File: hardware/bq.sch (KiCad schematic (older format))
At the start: 39 parts, among them Q11 BUK762R6-60E, Q12 BUK762R6-60E, Q13 Si2319DS, U1 bq7693002DBT, U2 BUK9Y43-60E

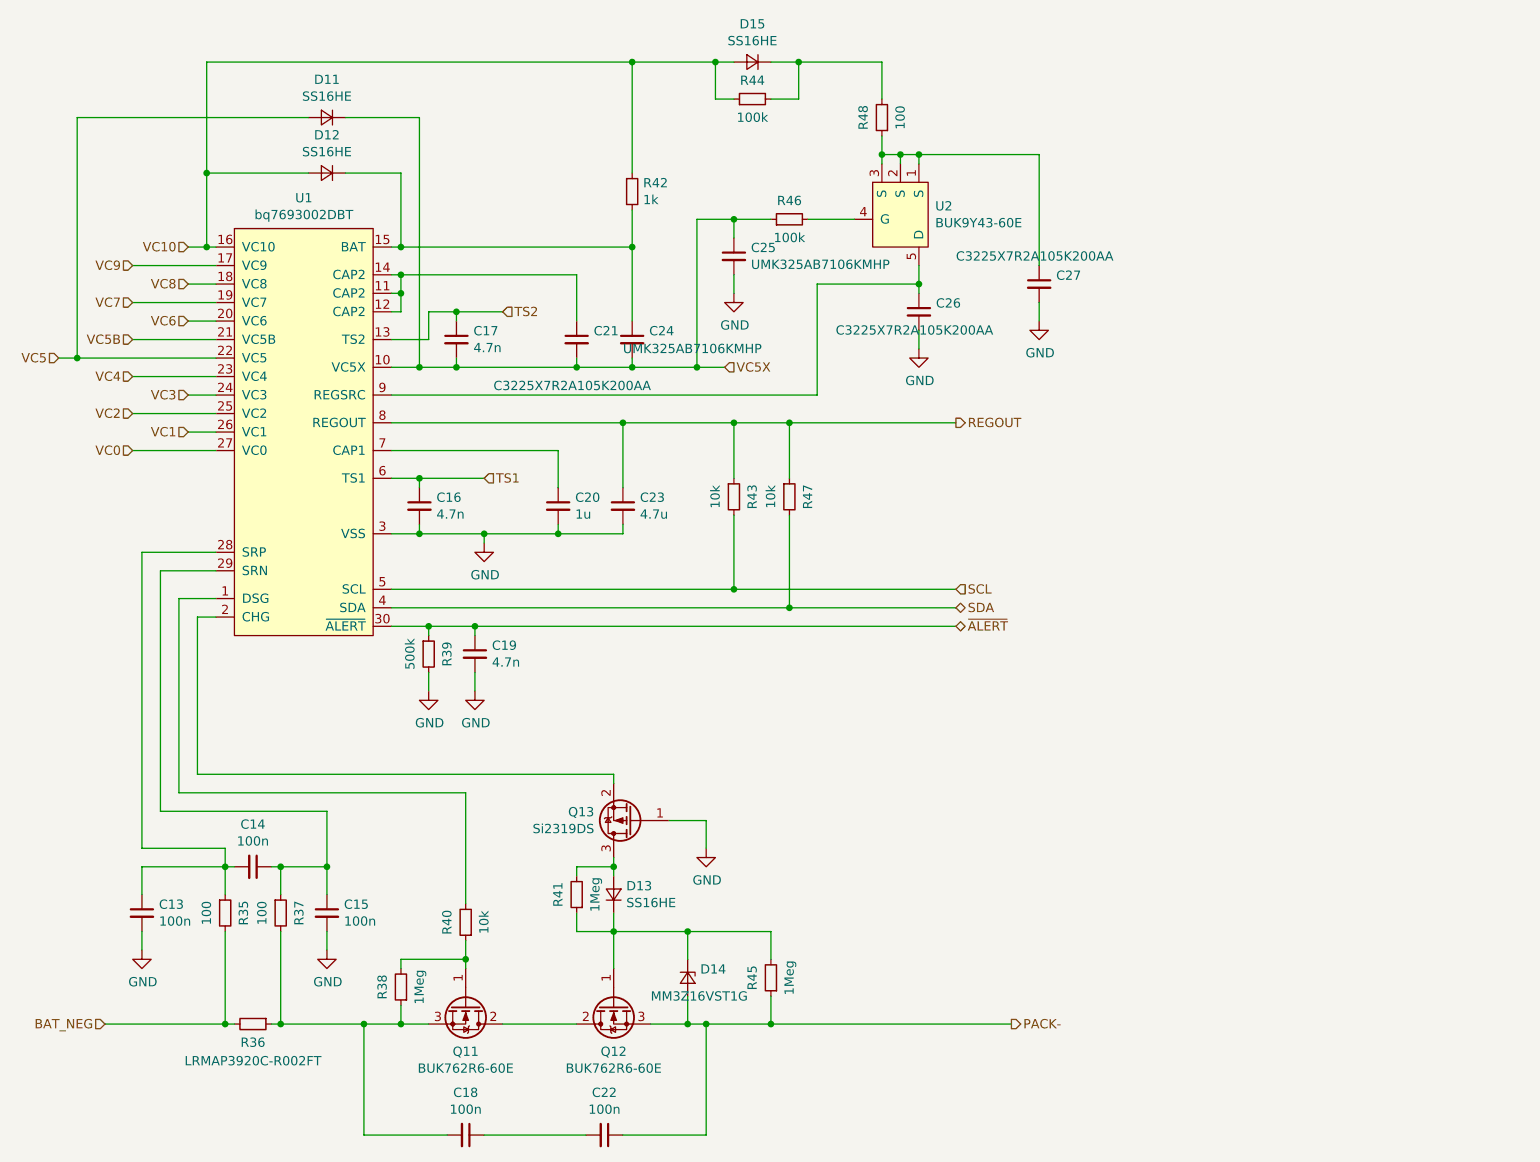
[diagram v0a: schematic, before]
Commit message: finish clean-up and part assignment
Signed-off-by: Ene Alexandru <ene.alexandru@gmail.com>
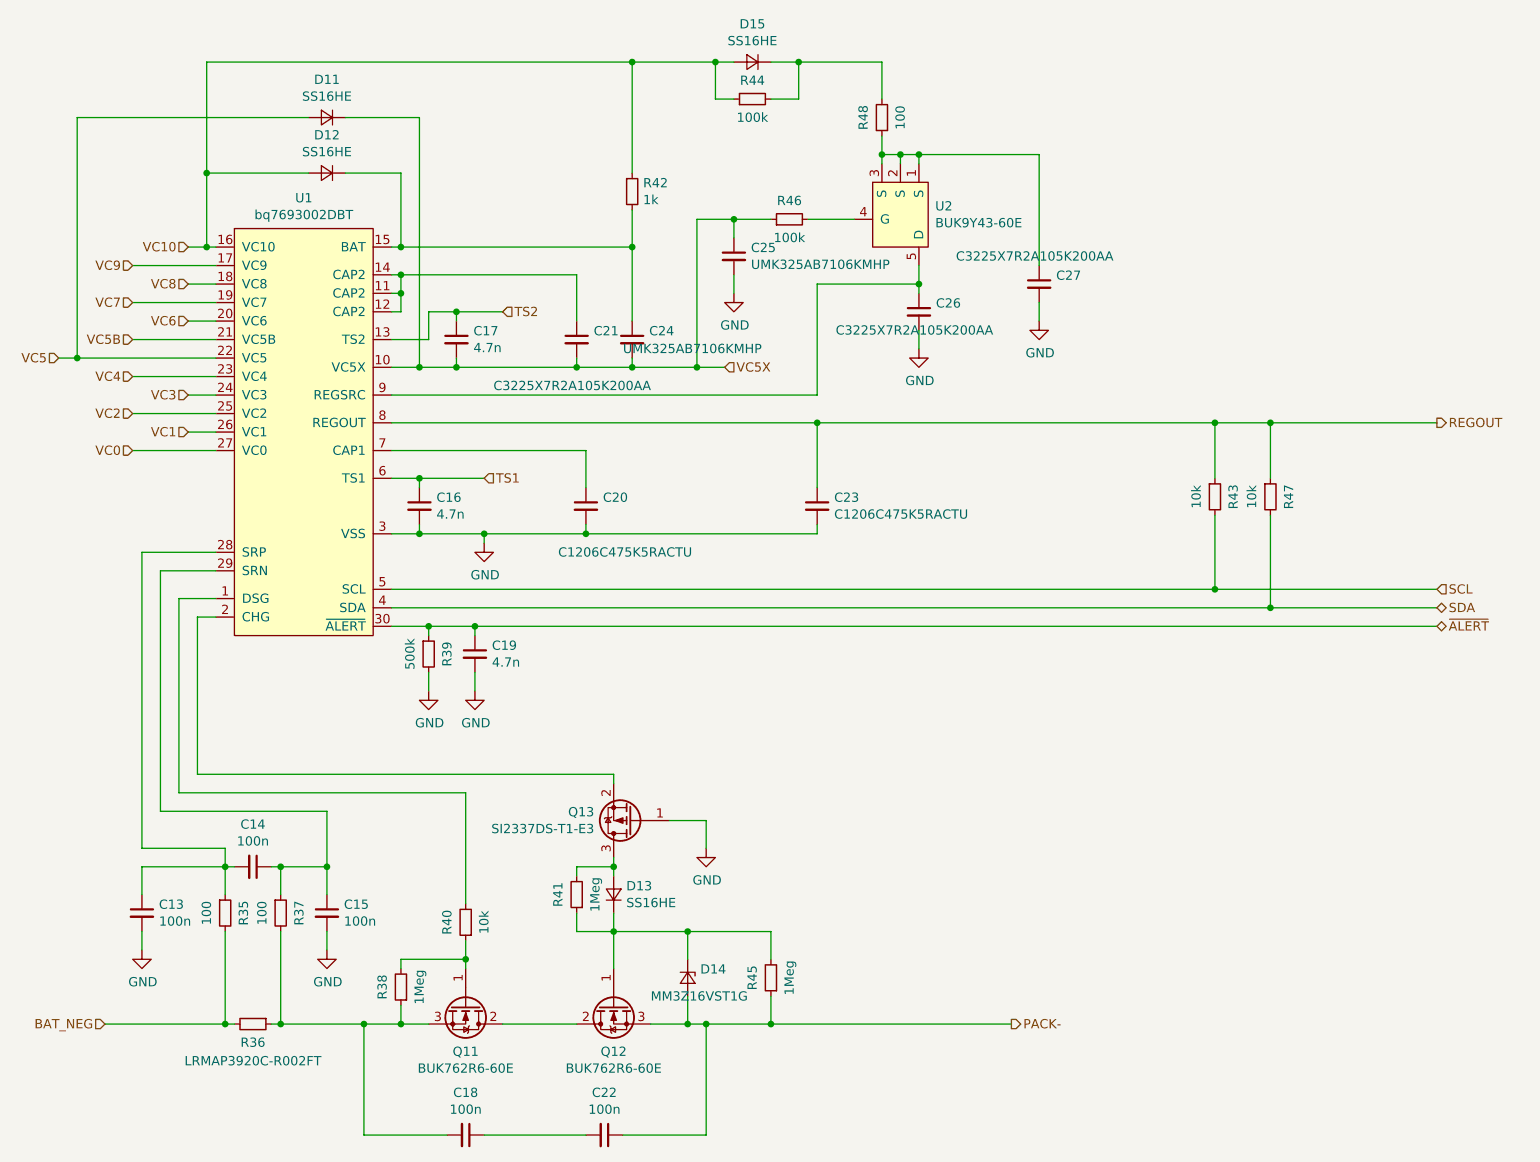
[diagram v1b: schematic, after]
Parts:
- C20: value 1u -> C1206C475K5RACTU
- C23: value 4.7u -> C1206C475K5RACTU
- Q13: value Si2319DS -> SI2337DS-T1-E3
- R36: footprint (none) -> bms_10s:LRMAP3920C-R002FT
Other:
- moved on the sheet: C20, C23, R43, R47
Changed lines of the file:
@@
 Wire Wire Line
 	5450 2050 5450 2100
-Wire Wire Line
-	2600 2800 3850 2800
 $Comp
 L Device:C_Small C16
@@
 L Device:C_Small C20
 U 1 1 5DF08E44
-P 3500 3250
-F 0 "C20" H 3592 3296 50  0000 L CNN
-F 1 "1u" H 3592 3205 50  0000 L CNN
-F 2 "Capacitor_SMD:C_0805_2012Metric_Pad1.15x1.40mm_HandSolder" H 3500 3250 50  0001 C CNN
-F 3 "~" H 3500 3250 50  0001 C CNN
-	1    3500 3250
+P 3650 3250
+F 0 "C20" H 3742 3296 50  0000 L CNN
+F 1 "C1206C475K5RACTU" H 3500 3000 50  0000 L CNN
+F 2 "Capacitor_SMD:C_0805_2012Metric_Pad1.15x1.40mm_HandSolder" H 3650 3250 50  0001 C CNN
+F 3 "~" H 3650 3250 50  0001 C CNN
+	1    3650 3250
 	1    0    0    -1
 $EndComp
@@
 	2750 3400 3100 3400
 Wire Wire Line
-	3500 3400 3500 3350
+	3650 3400 3650 3350
 Connection ~ 2750 3400
 $Comp
@@
 Wire Wire Line
 	3100 3450 3100 3400
-Connection ~ 3100 3400
-Wire Wire Line
-	3100 3400 3500 3400
-Wire Wire Line
-	2600 2950 3500 2950
-Wire Wire Line
-	3500 2950 3500 3150
+Wire Wire Line
+	3650 2950 3650 3150
 Wire Wire Line
 	2600 3100 2750 3100
@@
 L Device:C_Small C23
 U 1 1 5DF13B4E
-P 3850 3250
-F 0 "C23" H 3942 3296 50  0000 L CNN
-F 1 "4.7u" H 3942 3205 50  0000 L CNN
-F 2 "Capacitor_SMD:C_0805_2012Metric_Pad1.15x1.40mm_HandSolder" H 3850 3250 50  0001 C CNN
-F 3 "~" H 3850 3250 50  0001 C CNN
-	1    3850 3250
-	1    0    0    -1
-$EndComp
-Wire Wire Line
-	3850 3350 3850 3400
-Wire Wire Line
-	3850 3400 3500 3400
-Connection ~ 3500 3400
-Wire Wire Line
-	3850 3150 3850 2800
-Connection ~ 3850 2800
+P 4900 3250
+F 0 "C23" H 4992 3296 50  0000 L CNN
+F 1 "C1206C475K5RACTU" H 4992 3205 50  0000 L CNN
+F 2 "Capacitor_SMD:C_0805_2012Metric_Pad1.15x1.40mm_HandSolder" H 4900 3250 50  0001 C CNN
+F 3 "~" H 4900 3250 50  0001 C CNN
+	1    4900 3250
+	1    0    0    -1
+$EndComp
+Wire Wire Line
+	4900 3350 4900 3400
+Wire Wire Line
+	4900 3150 4900 2800
 $Comp
 L Device:R_Small R43
 U 1 1 5DF1F646
-P 4450 3200
-F 0 "R43" V 4550 3200 50  0000 C CNN
-F 1 "10k" V 4350 3200 50  0000 C CNN
-F 2 "Resistor_SMD:R_0805_2012Metric_Pad1.15x1.40mm_HandSolder" H 4450 3200 50  0001 C CNN
-F 3 "~" H 4450 3200 50  0001 C CNN
-	1    4450 3200
+P 7050 3200
+F 0 "R43" V 7150 3200 50  0000 C CNN
+F 1 "10k" V 6950 3200 50  0000 C CNN
+F 2 "Resistor_SMD:R_0805_2012Metric_Pad1.15x1.40mm_HandSolder" H 7050 3200 50  0001 C CNN
+F 3 "~" H 7050 3200 50  0001 C CNN
+	1    7050 3200
 	1    0    0    -1
 $EndComp
@@
 L Device:R_Small R47
 U 1 1 5DF1FDDA
-P 4750 3200
-F 0 "R47" V 4850 3200 50  0000 C CNN
-F 1 "10k" V 4650 3200 50  0000 C CNN
-F 2 "Resistor_SMD:R_0805_2012Metric_Pad1.15x1.40mm_HandSolder" H 4750 3200 50  0001 C CNN
-F 3 "~" H 4750 3200 50  0001 C CNN
-	1    4750 3200
-	1    0    0    -1
-$EndComp
-Wire Wire Line
-	3850 2800 4450 2800
-Wire Wire Line
-	2600 3700 4450 3700
-Wire Wire Line
-	4450 3100 4450 2800
-Connection ~ 4450 2800
-Wire Wire Line
-	4450 2800 4750 2800
-Wire Wire Line
-	4450 3300 4450 3700
-Connection ~ 4450 3700
-Wire Wire Line
-	4450 3700 5650 3700
-Wire Wire Line
-	2600 3800 4750 3800
-Wire Wire Line
-	4750 3300 4750 3800
-Connection ~ 4750 3800
-Wire Wire Line
-	4750 3800 5650 3800
-Wire Wire Line
-	4750 3100 4750 2800
-Connection ~ 4750 2800
-Wire Wire Line
-	4750 2800 5650 2800
+P 7350 3200
+F 0 "R47" V 7450 3200 50  0000 C CNN
+F 1 "10k" V 7250 3200 50  0000 C CNN
+F 2 "Resistor_SMD:R_0805_2012Metric_Pad1.15x1.40mm_HandSolder" H 7350 3200 50  0001 C CNN
+F 3 "~" H 7350 3200 50  0001 C CNN
+	1    7350 3200
+	1    0    0    -1
+$EndComp
+Wire Wire Line
+	7050 3100 7050 2800
+Connection ~ 7050 2800
+Wire Wire Line
+	7050 2800 7350 2800
+Wire Wire Line
+	7050 3300 7050 3700
+Connection ~ 7050 3700
+Wire Wire Line
+	7050 3700 8250 3700
+Wire Wire Line
+	7350 3300 7350 3800
+Connection ~ 7350 3800
+Wire Wire Line
+	7350 3800 8250 3800
+Wire Wire Line
+	7350 3100 7350 2800
+Connection ~ 7350 2800
+Wire Wire Line
+	7350 2800 8250 2800
 $Comp
 L Device:R_Small R39
@@
 Wire Wire Line
 	3050 3950 3050 3900
-Connection ~ 3050 3900
-Wire Wire Line
-	3050 3900 5650 3900
 $Comp
 L Device:R_Small R36
@@
 F 0 "R36" V 1950 6050 50  0000 C CNN
 F 1 "LRMAP3920C-R002FT" V 2050 6050 50  0000 C CNN
-F 2 "" H 1850 6050 50  0001 C CNN
+F 2 "bms_10s:LRMAP3920C-R002FT" H 1850 6050 50  0001 C CNN
 F 3 "~" H 1850 6050 50  0001 C CNN
 	1    1850 6050
@@
 Text HLabel 4400 2500 2    50   Input ~ 0
 VC5X
-Text HLabel 5650 2800 2    50   Output ~ 0
+Text HLabel 8250 2800 2    50   Output ~ 0
 REGOUT
-Text HLabel 5650 3700 2    50   Input ~ 0
+Text HLabel 8250 3700 2    50   Input ~ 0
 SCL
-Text HLabel 5650 3800 2    50   BiDi ~ 0
+Text HLabel 8250 3800 2    50   BiDi ~ 0
 SDA
-Text HLabel 5650 3900 2    50   BiDi ~ 0
+Text HLabel 8250 3900 2    50   BiDi ~ 0
 ~ALERT
 $Comp
@@
 P 3900 4950
 F 0 "Q13" H 4105 4904 50  0000 L CNN
-F 1 "Si2319DS" H 4105 4995 50  0000 L CNN
+F 1 "SI2337DS-T1-E3" H 4105 4995 50  0000 L CNN
 F 2 "Package_TO_SOT_SMD:SOT-23" H 4100 5050 50  0001 C CNN
 F 3 "~" H 3900 4950 50  0001 C CNN
@@
 Wire Wire Line
 	5450 1350 5350 1350
+Wire Wire Line
+	3100 3400 3650 3400
+Connection ~ 3100 3400
+Wire Wire Line
+	2600 2950 3650 2950
+Wire Wire Line
+	2600 2800 4900 2800
+Wire Wire Line
+	3650 3400 4900 3400
+Connection ~ 3650 3400
+Wire Wire Line
+	2600 3700 7050 3700
+Wire Wire Line
+	2600 3800 7350 3800
+Wire Wire Line
+	3050 3900 8250 3900
+Connection ~ 3050 3900
+Wire Wire Line
+	4900 2800 7050 2800
+Connection ~ 4900 2800
 $EndSCHEMATC

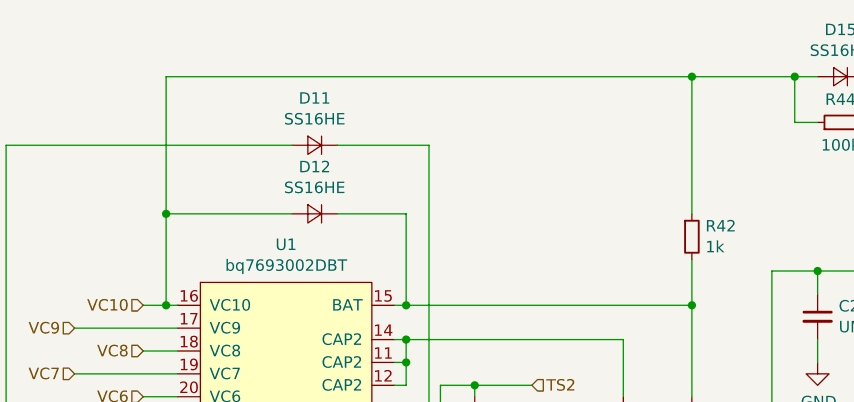
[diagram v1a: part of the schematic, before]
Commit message: almost ready for pcb, needs revision
Signed-off-by: Ene Alexandru <ene.alexandru@gmail.com>
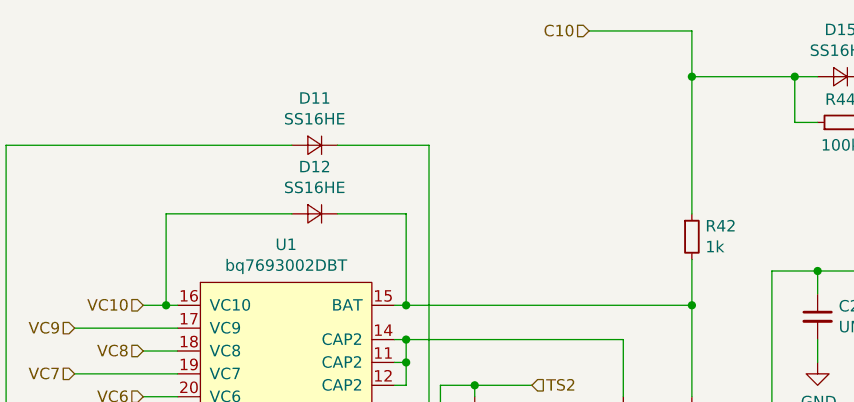
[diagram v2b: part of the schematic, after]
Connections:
- net VC10: no longer D15.2 (A), R42.1, R44.1
- new net C10: D15.2 (A), R42.1, R44.1
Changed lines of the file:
@@
 $Descr A4 11693 8268
 encoding utf-8
-Sheet 3 4
+Sheet 4 4
 Title ""
 Date ""
@@
 Connection ~ 3900 1850
 Wire Wire Line
-	1600 1450 1600 850
-Wire Wire Line
-	1600 850  3900 850
-Wire Wire Line
 	3900 850  3900 1450
-Connection ~ 1600 1450
 $Comp
 L Device:D_Small D15
@@
 Wire Wire Line
 	4450 850  4350 850
-Connection ~ 3900 850
 Wire Wire Line
 	4450 1050 4350 1050
@@
 	4900 2800 7050 2800
 Connection ~ 4900 2800
+Connection ~ 3900 850
+Text HLabel 3450 650  0    50   Input ~ 0
+C10
+Wire Wire Line
+	3900 650  3900 850
+Wire Wire Line
+	3450 650  3900 650
 $EndSCHEMATC
